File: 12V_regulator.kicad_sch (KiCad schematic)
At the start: 63 parts

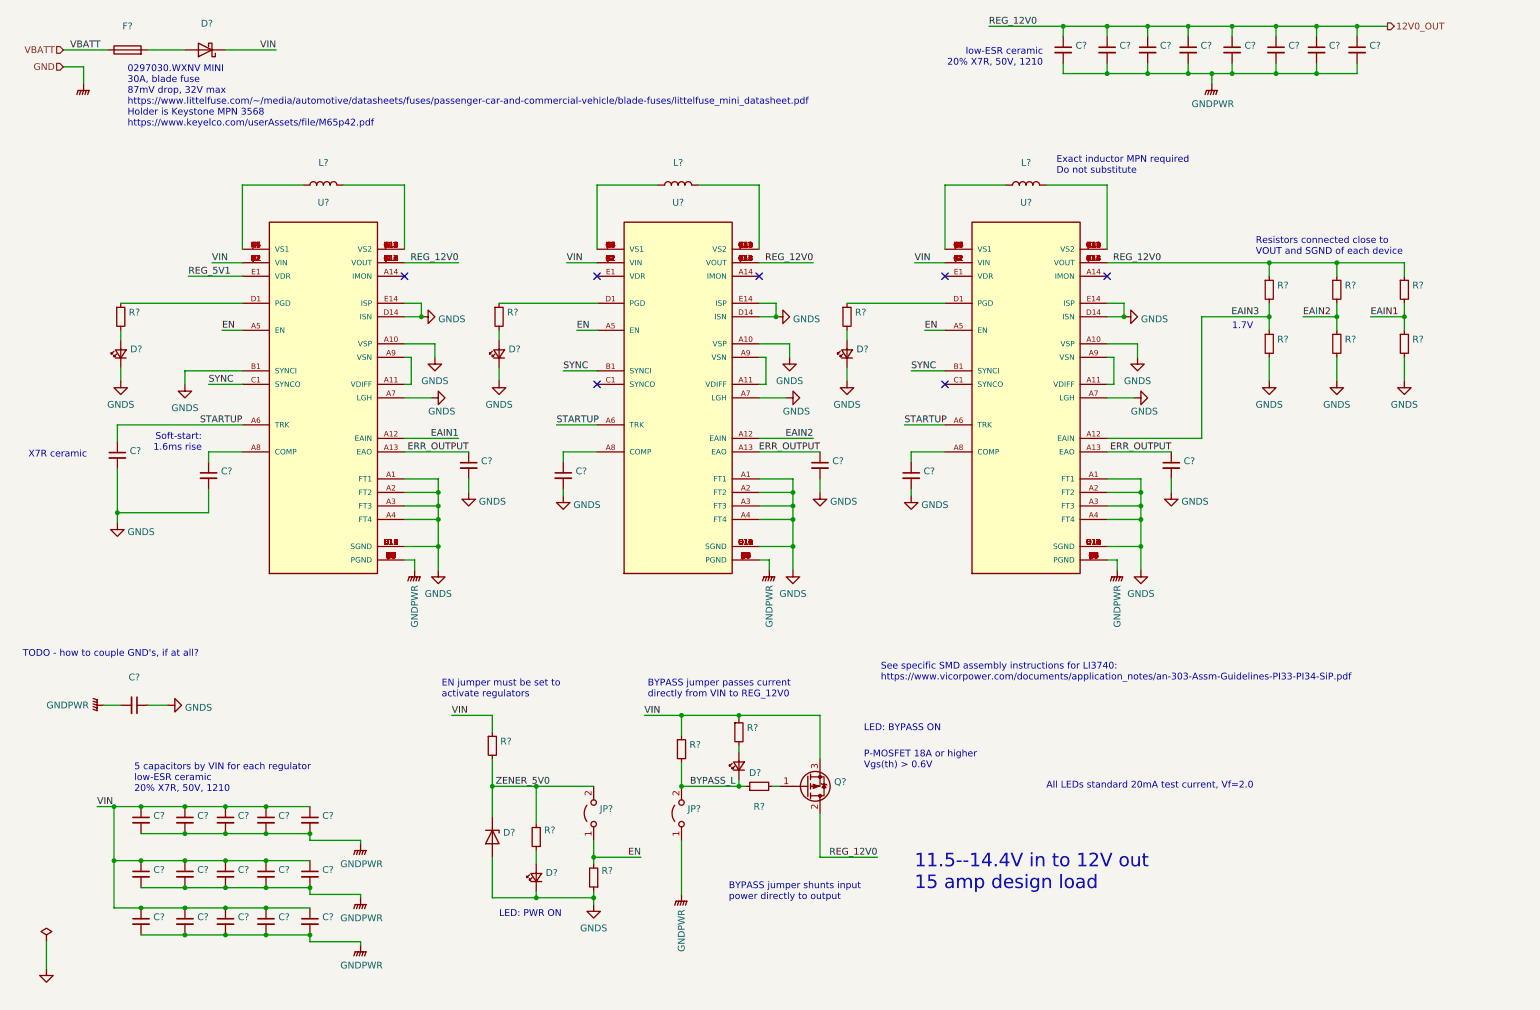
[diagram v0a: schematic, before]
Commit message: A bit more cleanup on that older 12V regulator
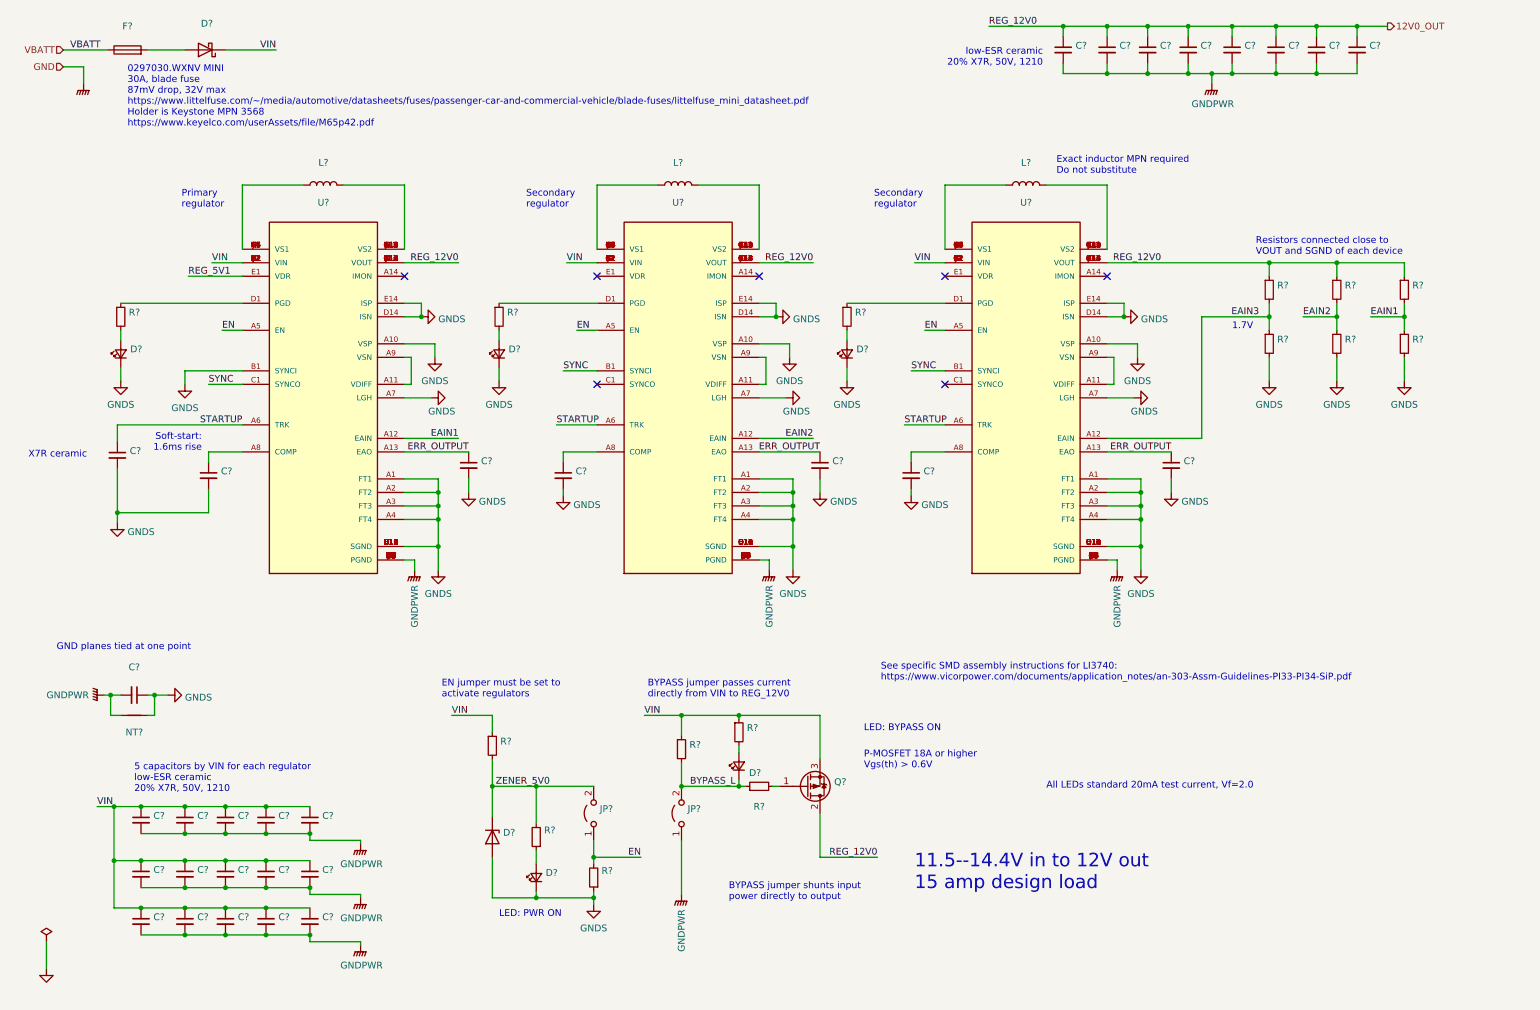
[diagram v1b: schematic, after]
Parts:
- added NT?: (no value), symbol Device:NetTie_2
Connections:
- net GNDPWR: now also NT?.1
- net GNDS: now also NT?.2
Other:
- note added: "GND planes tied at one point"
- note added: "Primary regulator"
- note added: "Secondary regulator"
- note removed: "TODO - how to couple GND's, if at all?"
- moved on the sheet: C?
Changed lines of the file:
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@@
   (junction (at 241.935 15.24) (diameter 0) (color 0 0 0 0)
   )
+  (junction (at 39.37 140.97) (diameter 0) (color 0 0 0 0)
+  )
   (junction (at 121.92 171.45) (diameter 0) (color 0 0 0 0)
   )
@@
   )
   (junction (at 261.62 59.69) (diameter 0) (color 0 0 0 0)
+  )
+  (junction (at 31.115 140.97) (diameter 0) (color 0 0 0 0)
   )
   (junction (at 224.79 113.03) (diameter 0) (color 0 0 0 0)
@@
     (stroke (width 0) (type default) (color 0 0 0 0))
   )
-  (wire (pts (xy 38.1 142.875) (xy 41.91 142.875))
+  (wire (pts (xy 38.1 140.97) (xy 39.37 140.97))
     (stroke (width 0) (type default) (color 0 0 0 0))
   )
@@
     (stroke (width 0) (type default) (color 0 0 0 0))
   )
+  (wire (pts (xy 31.115 140.97) (xy 33.02 140.97))
+    (stroke (width 0) (type default) (color 0 0 0 0))
+  )
   (wire (pts (xy 68.58 186.055) (xy 68.58 187.325))
     (stroke (width 0) (type default) (color 0 0 0 0))
@@
     (stroke (width 0) (type default) (color 0 0 0 0))
   )
+  (wire (pts (xy 33.02 144.78) (xy 31.115 144.78))
+    (stroke (width 0) (type default) (color 0 0 0 0))
+  )
   (wire (pts (xy 22.225 19.685) (xy 30.48 19.685))
     (stroke (width 0) (type default) (color 0 0 0 0))
@@
     (stroke (width 0) (type default) (color 0 0 0 0))
   )
+  (wire (pts (xy 38.1 144.78) (xy 39.37 144.78))
+    (stroke (width 0) (type default) (color 0 0 0 0))
+  )
   (wire (pts (xy 49.53 106.68) (xy 49.53 102.235))
     (stroke (width 0) (type default) (color 0 0 0 0))
@@
     (stroke (width 0) (type default) (color 0 0 0 0))
   )
-  (wire (pts (xy 29.845 142.875) (xy 33.02 142.875))
+  (wire (pts (xy 29.845 140.97) (xy 31.115 140.97))
+    (stroke (width 0) (type default) (color 0 0 0 0))
+  )
+  (wire (pts (xy 39.37 144.78) (xy 39.37 140.97))
+    (stroke (width 0) (type default) (color 0 0 0 0))
+  )
+  (wire (pts (xy 39.37 140.97) (xy 41.91 140.97))
     (stroke (width 0) (type default) (color 0 0 0 0))
   )
@@
     (stroke (width 0) (type default) (color 0 0 0 0))
   )
+  (wire (pts (xy 31.115 144.78) (xy 31.115 140.97))
+    (stroke (width 0) (type default) (color 0 0 0 0))
+  )
   (wire (pts (xy 33.02 67.31) (xy 55.88 67.31))
     (stroke (width 0) (type default) (color 0 0 0 0))
@@
   )
   (text "LED: PWR ON" (at 104.14 182.88 0)
+    (effects (font (size 1.27 1.27)) (justify left bottom))
+  )
+  (text "Primary\nregulator" (at 44.45 49.53 0)
     (effects (font (size 1.27 1.27)) (justify left bottom))
   )
@@
     (effects (font (size 1.27 1.27)) (justify left bottom))
   )
-  (text "TODO - how to couple GND's, if at all?" (at 14.605 133.985 0)
-    (effects (font (size 1.27 1.27)) (justify left bottom))
-  )
   (text "Soft-start: \n1.6ms rise\n" (at 48.26 95.25 180)
     (effects (font (size 1.27 1.27)) (justify right bottom))
@@
     (effects (font (size 1.27 1.27)) (justify left bottom))
   )
+  (text "Secondary\nregulator" (at 174.625 49.53 0)
+    (effects (font (size 1.27 1.27)) (justify left bottom))
+  )
   (text "Exact inductor MPN required\nDo not substitute" (at 208.915 43.18 0)
     (effects (font (size 1.27 1.27)) (justify left bottom))
@@
     (effects (font (size 1.27 1.27)) (justify left bottom))
   )
+  (text "Secondary\nregulator" (at 109.22 49.53 0)
+    (effects (font (size 1.27 1.27)) (justify left bottom))
+  )
   (text "11.5--14.4V in to 12V out\n15 amp design load" (at 182.245 177.8 0)
     (effects (font (size 2.54 2.54)) (justify left bottom))
@@
   (text "BYPASS jumper shunts input\npower directly to output"
     (at 147.32 179.705 0)
+    (effects (font (size 1.27 1.27)) (justify left bottom))
+  )
+  (text "GND planes tied at one point" (at 20.955 132.715 0)
     (effects (font (size 1.27 1.27)) (justify left bottom))
   )
@@
     (pin "2")
   )
+  (symbol (lib_id "Device:NetTie_2") (at 35.56 144.78 0) (unit 1)
+    (in_bom yes) (on_board yes)
+    (property "Reference" "NT?" (id 0) (at 35.56 147.955 0))
+    (property "Value" "" (id 1) (at 35.56 146.05 0))
+    (property "Footprint" "" (id 2) (at 35.56 144.78 0)
+      (effects (font (size 1.27 1.27)) hide)
+    )
+    (property "Datasheet" "~" (id 3) (at 35.56 144.78 0)
+      (effects (font (size 1.27 1.27)) hide)
+    )
+    (pin "1")
+    (pin "2")
+  )
   (symbol (lib_id "power:GNDPWR") (at 220.345 117.475 0) (unit 1)
     (in_bom yes) (on_board yes)
@@
     (pin "2")
   )
-  (symbol (lib_id "Device:C_Small") (at 35.56 142.875 270) (unit 1)
-    (in_bom yes) (on_board yes) (fields_autoplaced)
-    (property "Reference" "C?" (id 0) (at 35.5536 137.6131 90))
-    (property "Value" "" (id 1) (at 35.5536 140.15 90))
-    (property "Footprint" "" (id 2) (at 35.56 142.875 0)
-      (effects (font (size 1.27 1.27)) hide)
-    )
-    (property "Datasheet" "~" (id 3) (at 35.56 142.875 0)
+  (symbol (lib_id "Device:C_Small") (at 35.56 140.97 270) (unit 1)
+    (in_bom yes) (on_board yes) (fields_autoplaced)
+    (property "Reference" "C?" (id 0) (at 35.5536 135.7081 90))
+    (property "Value" "" (id 1) (at 35.5536 138.245 90))
+    (property "Footprint" "" (id 2) (at 35.56 140.97 0)
+      (effects (font (size 1.27 1.27)) hide)
+    )
+    (property "Datasheet" "~" (id 3) (at 35.56 140.97 0)
       (effects (font (size 1.27 1.27)) hide)
     )
@@
     (pin "2")
   )
-  (symbol (lib_id "power:GNDS") (at 41.91 142.875 90) (unit 1)
-    (in_bom yes) (on_board yes) (fields_autoplaced)
-    (property "Reference" "#PWR?" (id 0) (at 48.26 142.875 0)
-      (effects (font (size 1.27 1.27)) hide)
-    )
-    (property "Value" "GNDS" (id 1) (at 45.085 143.3088 90)
+  (symbol (lib_id "power:GNDS") (at 41.91 140.97 90) (unit 1)
+    (in_bom yes) (on_board yes) (fields_autoplaced)
+    (property "Reference" "#PWR?" (id 0) (at 48.26 140.97 0)
+      (effects (font (size 1.27 1.27)) hide)
+    )
+    (property "Value" "GNDS" (id 1) (at 45.085 141.4038 90)
       (effects (font (size 1.27 1.27)) (justify right))
     )
-    (property "Footprint" "" (id 2) (at 41.91 142.875 0)
-      (effects (font (size 1.27 1.27)) hide)
-    )
-    (property "Datasheet" "" (id 3) (at 41.91 142.875 0)
+    (property "Footprint" "" (id 2) (at 41.91 140.97 0)
+      (effects (font (size 1.27 1.27)) hide)
+    )
+    (property "Datasheet" "" (id 3) (at 41.91 140.97 0)
       (effects (font (size 1.27 1.27)) hide)
     )
@@
     (pin "2")
   )
-  (symbol (lib_id "power:GNDPWR") (at 29.845 142.875 270) (unit 1)
+  (symbol (lib_id "power:GNDPWR") (at 29.845 140.97 270) (unit 1)
     (in_bom yes) (on_board yes)
-    (property "Reference" "#PWR?" (id 0) (at 24.765 142.875 0)
-      (effects (font (size 1.27 1.27)) hide)
-    )
-    (property "Value" "GNDPWR" (id 1) (at 19.05 142.875 90)
-      (effects (font (size 1.27 1.27)) (justify left))
-    )
-    (property "Footprint" "" (id 2) (at 28.575 142.875 0)
-      (effects (font (size 1.27 1.27)) hide)
-    )
-    (property "Datasheet" "" (id 3) (at 28.575 142.875 0)
-      (effects (font (size 1.27 1.27)) hide)
-    )
+    (property "Reference" "#PWR?" (id 0) (at 24.765 140.97 0)
+      (effects (font (size 1.27 1.27)) hide)
+    )
+    (property "Value" "GNDPWR" (id 1) (at 19.05 140.97 90)
+      (effects (font (size 1.27 1.27)) (justify left))
+    )
+    (property "Footprint" "" (id 2) (at 28.575 140.97 0)
+      (effects (font (size 1.27 1.27)) hide)
+    )
+    (property "Datasheet" "" (id 3) (at 28.575 140.97 0)
+      (effects (font (size 1.27 1.27)) hide)
+    )

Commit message: Clear the decks for new 12V regulator design
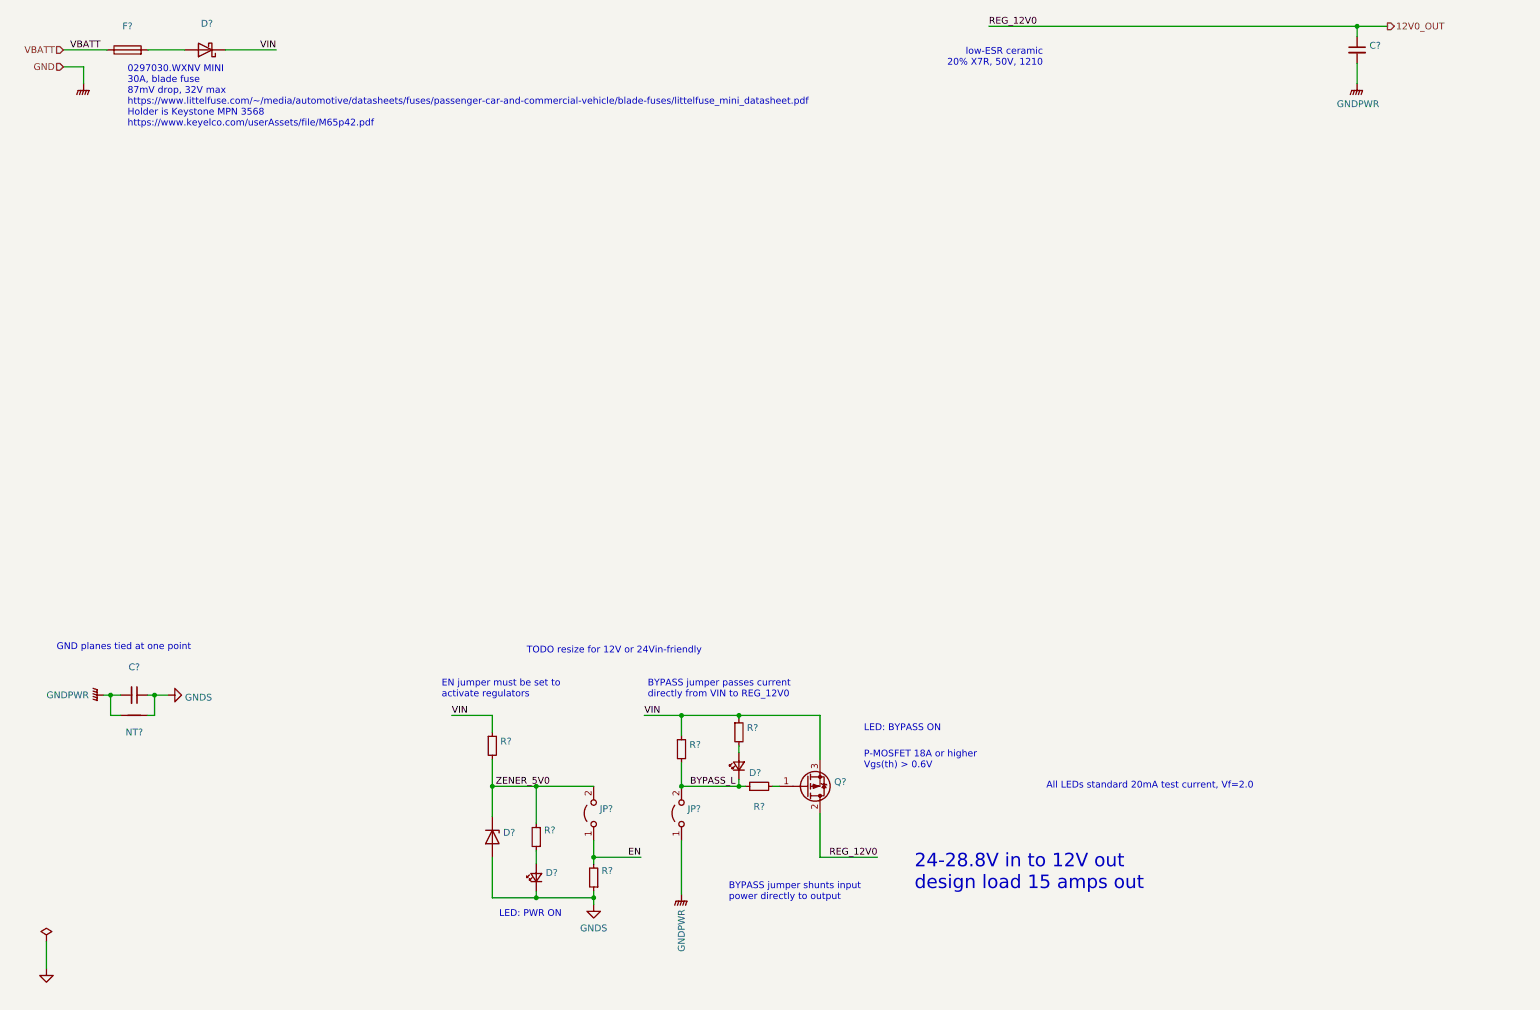
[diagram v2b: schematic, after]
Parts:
- removed C? (x29): (no value), symbol Device:C_Small
- removed D? (x3): (no value), symbol Device:LED_Small
- removed L? (x3): (no value), symbol Device:L
- removed R? (x9): (no value), symbol Device:R_Small
- removed U? (x3): (no value), symbol Aaron-Regulators:PI3740-00-LGIZ
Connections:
- no-connect marks 7 -> 0
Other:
- note added: "24-28.8V in to 12V out design load 15 amps out"
- note added: "TODO resize for 12V or 24Vin-friendly"
- note removed: "1.7V"
- note removed: "11.5--14.4V in to 12V out 15 amp design load"
- note removed: "5 capacitors by VIN for each regulator low-ESR ceramic 20% X7R, 50V, 1210"
- note removed: "Exact inductor MPN required Do not substitute"
- note removed: "Primary regulator"
- note removed: "Resistors connected close to VOUT and SGND of each device"
- note removed: "Secondary regulator"
- note removed: "See specific SMD assembly instructions for LI3740: https://www.vicorpower.com/documents/application_notes/an-303-Assm-Guidelines-PI33-PI34-SiP.pdf"
- note removed: "Soft-start: 1.6ms rise"
- note removed: "X7R ceramic"
